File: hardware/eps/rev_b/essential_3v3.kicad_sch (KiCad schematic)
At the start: 16 parts, among them U400 LMR51635XDDCR

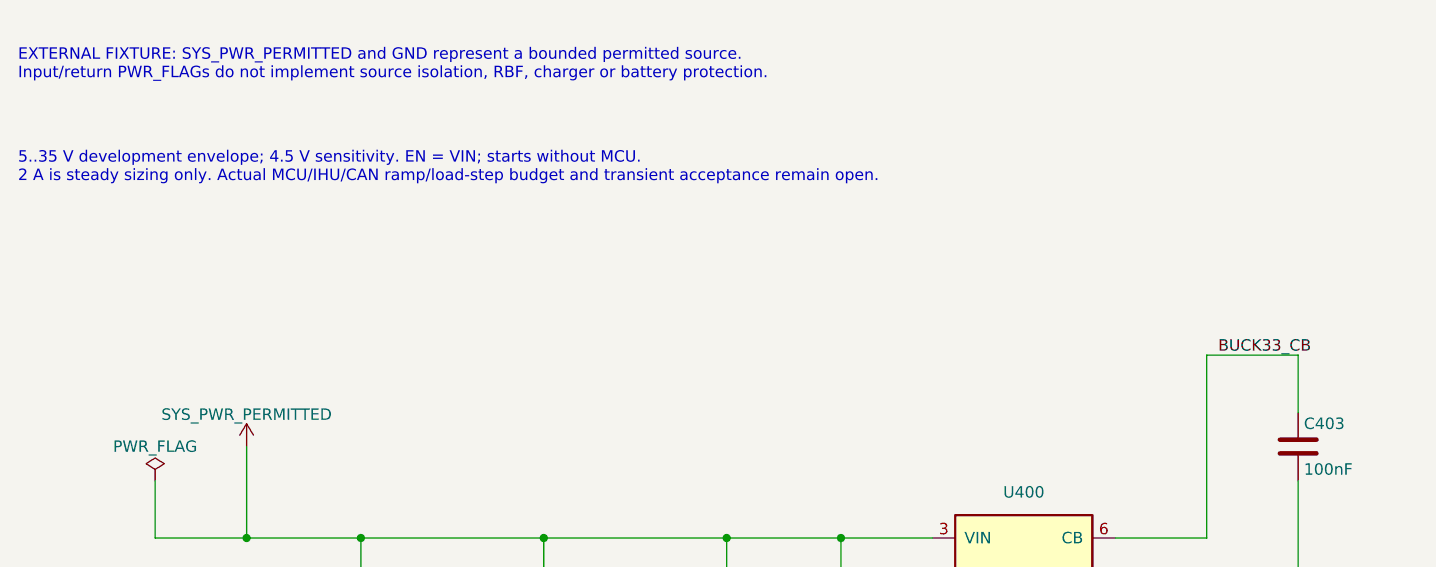
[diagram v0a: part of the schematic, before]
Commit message: Integrate LTC4162 charger PowerPath and thermistor interface into EPS Rev B
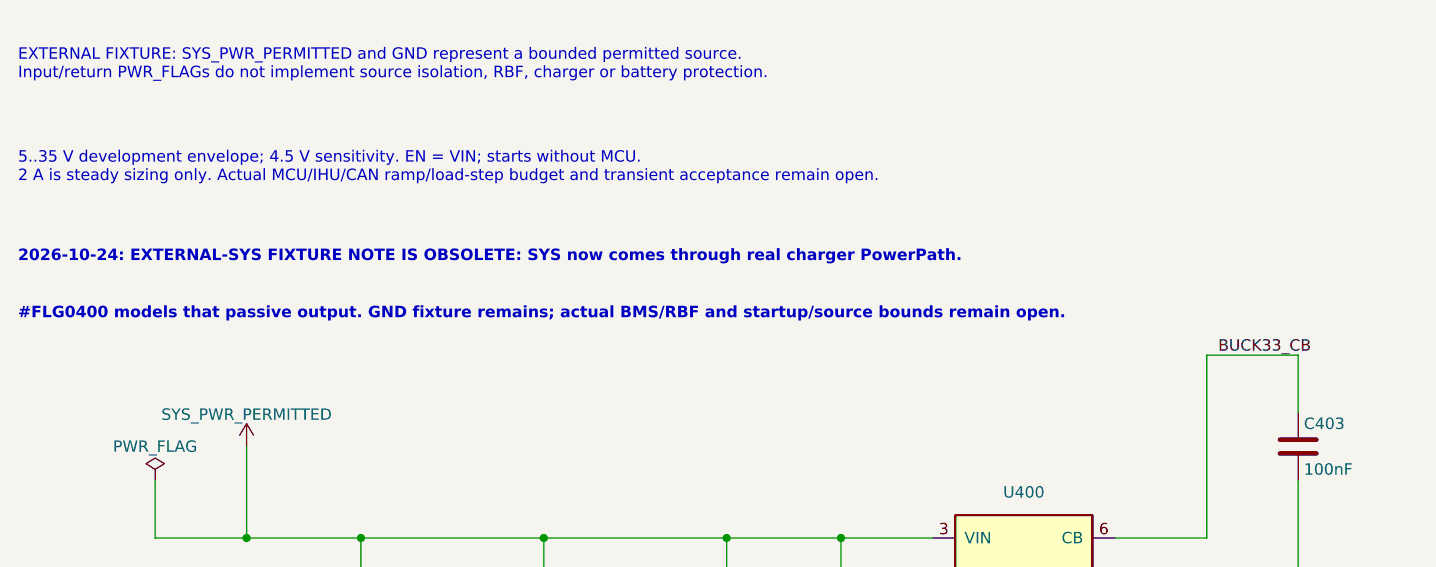
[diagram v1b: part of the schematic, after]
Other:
- note added: "#FLG0400 models that passive output. GND fixture remains; actual BMS/RBF and startup/source bounds remain open."
- note added: "2026-10-24: EXTERNAL-SYS FIXTURE NOTE IS OBSOLETE: SYS now comes through real charger PowerPath."
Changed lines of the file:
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@@
     (effects (font (size 1.27 1.27)) (justify left bottom))
+  )
+  (text "2026-10-24: EXTERNAL-SYS FIXTURE NOTE IS OBSOLETE: SYS now comes through real charger PowerPath."
+    (at 25.4 55.88 0)
+    (effects (font (size 1.27 1.27) (bold yes)) (justify left bottom))
+  )
+  (text "#FLG0400 models that passive output. GND fixture remains; actual BMS/RBF and startup/source bounds remain open."
+    (at 25.4 62.23 0)
+    (effects (font (size 1.27 1.27) (bold yes)) (justify left bottom))
   )
 	(symbol
@@
 			)
 		)
-	)
+		(property "SourceDisposition" "Actual passive charger PowerPath output; supersedes earlier external SYS fixture"
+			(at 40.64 80.01 0)
+			(hide yes)
+			(effects
+				(font
+					(size 1.27 1.27)
+				)
+			)
+		))
 	(symbol
 		(lib_id "power:GND")
